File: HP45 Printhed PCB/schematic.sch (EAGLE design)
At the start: 38 parts, among them J1 87224-1, J10 640454-5, J2 87224-1, J3 87224-1, J4 87224-1, J5 87224-1, J6 87224-1, J7 87224-1, J8 87224-1, J9 87224-1, P1 282837-2, Q1 L78M05CDT, U11 DMG1013UWQ-7, U12 DMG1013UWQ-7, U13 DMG1013UWQ-7, U14 DMG1013UWQ-7, U15 DMG1013UWQ-7, U16 DMG1013UWQ-7, U17 DMG1013UWQ-7, U18 DMG1013UWQ-7, U2 CD4504BPWE4, U3 CD4504BPWE4

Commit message: PCB
Completed board 1.0
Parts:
- added R11, R12: 1000Ω, resistor:R-US_R0603
- C1, C2, C3, C4, C5: device capacitor-wima:C2,5-3 -> rcl:C-USC0603
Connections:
- net PIC_MCLR renamed PICKIT_MCLR
- removed net PIC_VDD: C5.1, J10.2, PIC.VDD
- removed net VO: C2.1, Q1.OUT, R2.2
- new net N$12: PIC.RB5, PIC.RC2, PIC.RC4/D-, PIC.RC5/D+, PIC.RC6, PIC.RC7, R12.1
- new net N$3: PIC.RA4, PIC.RA5, PIC.RA6, PIC.RA7, PIC.RB0, R11.2
- new net PICKIT_VDD: C2.1, C5.1, J10.2, PIC.VDD, Q1.OUT, R2.2
- net GND: now also R11.1, R12.2, U2.EIN, U2.FIN, U3.EIN, U3.FIN

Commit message: GRB File
GRB File made and some changes to PCB (Spring loaded pins, names)
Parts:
- C1, C2, C4, C5: MPN (none) -> B32529C0104J000; OC_NEWARK (none) -> 26M8219
- C3, L78M05CDT, MOSFET1, MOSFET3, MOSFET4, MOSFET5, MOSFET6, MOSFET7, MOSFET8, P1, PIC18F, PROGRAMMER, R1, R10, R11, R12, R2, R3, R4, R5, R6, R7, R8, R9, U11, VSHIFTER1, VSHIFTER2: OC_NEWARK (none) -> unknown
- J1, J2, J3, J4, J5, J6, J7, J8, J9: value 87224-1 -> 0926-1-15-20-75-14-11-0; device 87224-1:87224-1 -> 0926-1-15-20-75-14-11-0:0926-1-15-20-75-14-11-0; OC_NEWARK (none) -> unknown
- renumbered J10 to PROGRAMMER, PIC to PIC18F, Q1 to L78M05CDT, U12 to MOSFET4, U13 to MOSFET6, U14 to MOSFET8, U15 to MOSFET1, U16 to MOSFET3, U17 to MOSFET5, U18 to MOSFET7, U2 to VSHIFTER1, U3 to VSHIFTER2

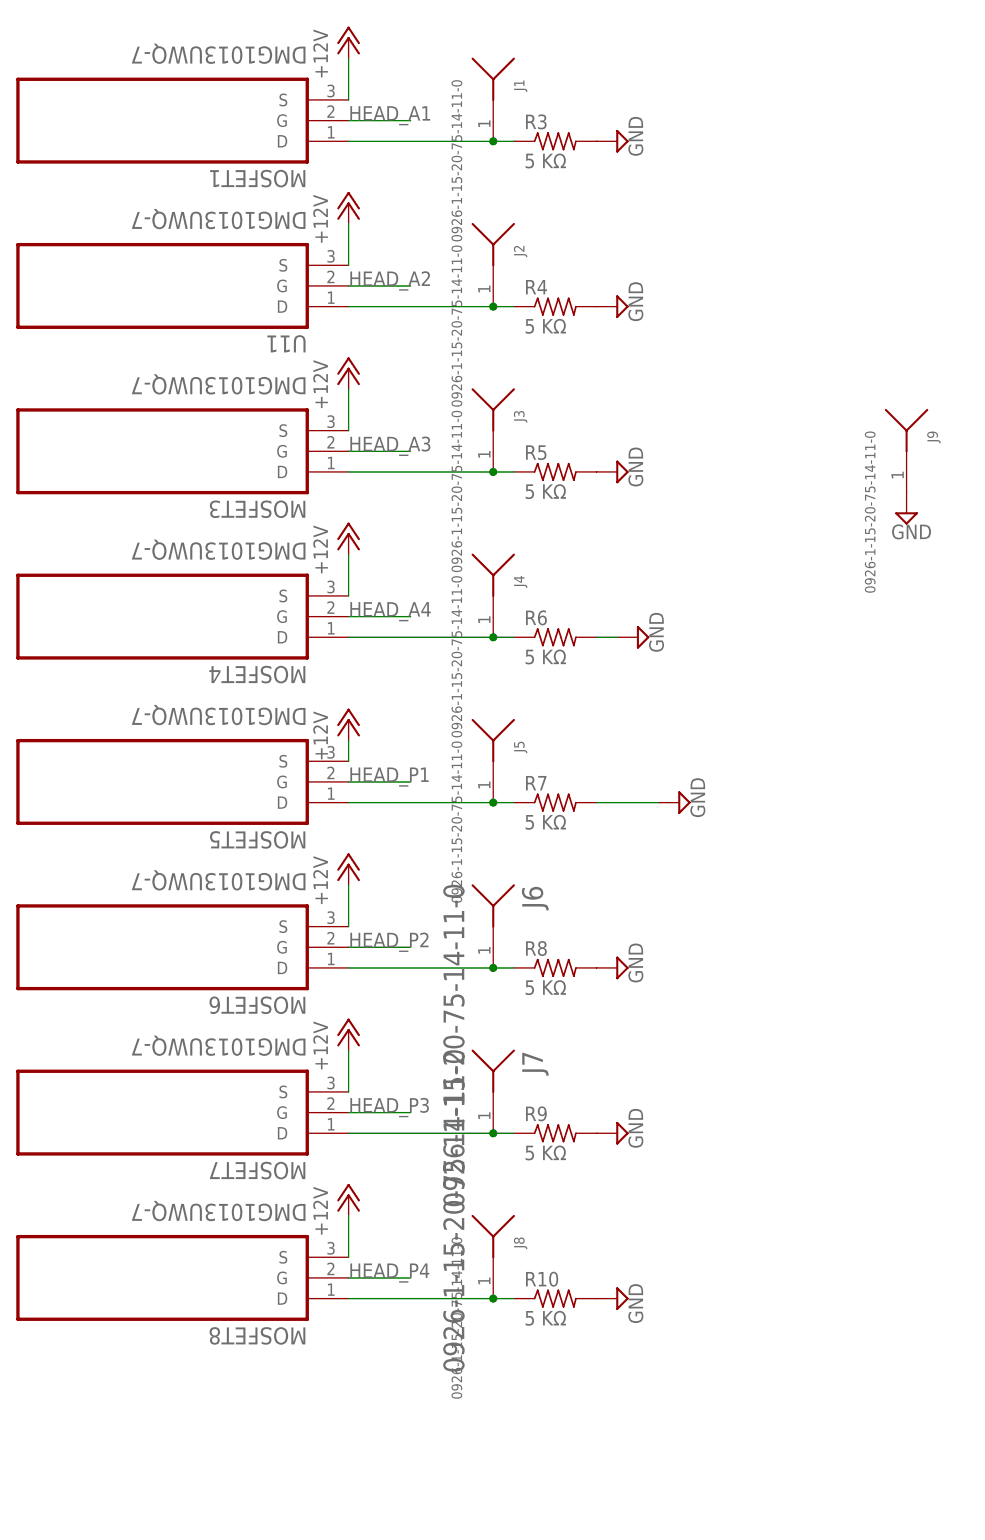
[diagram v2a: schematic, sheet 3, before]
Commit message: PCB Changes
Revised pinheads, modified libraries
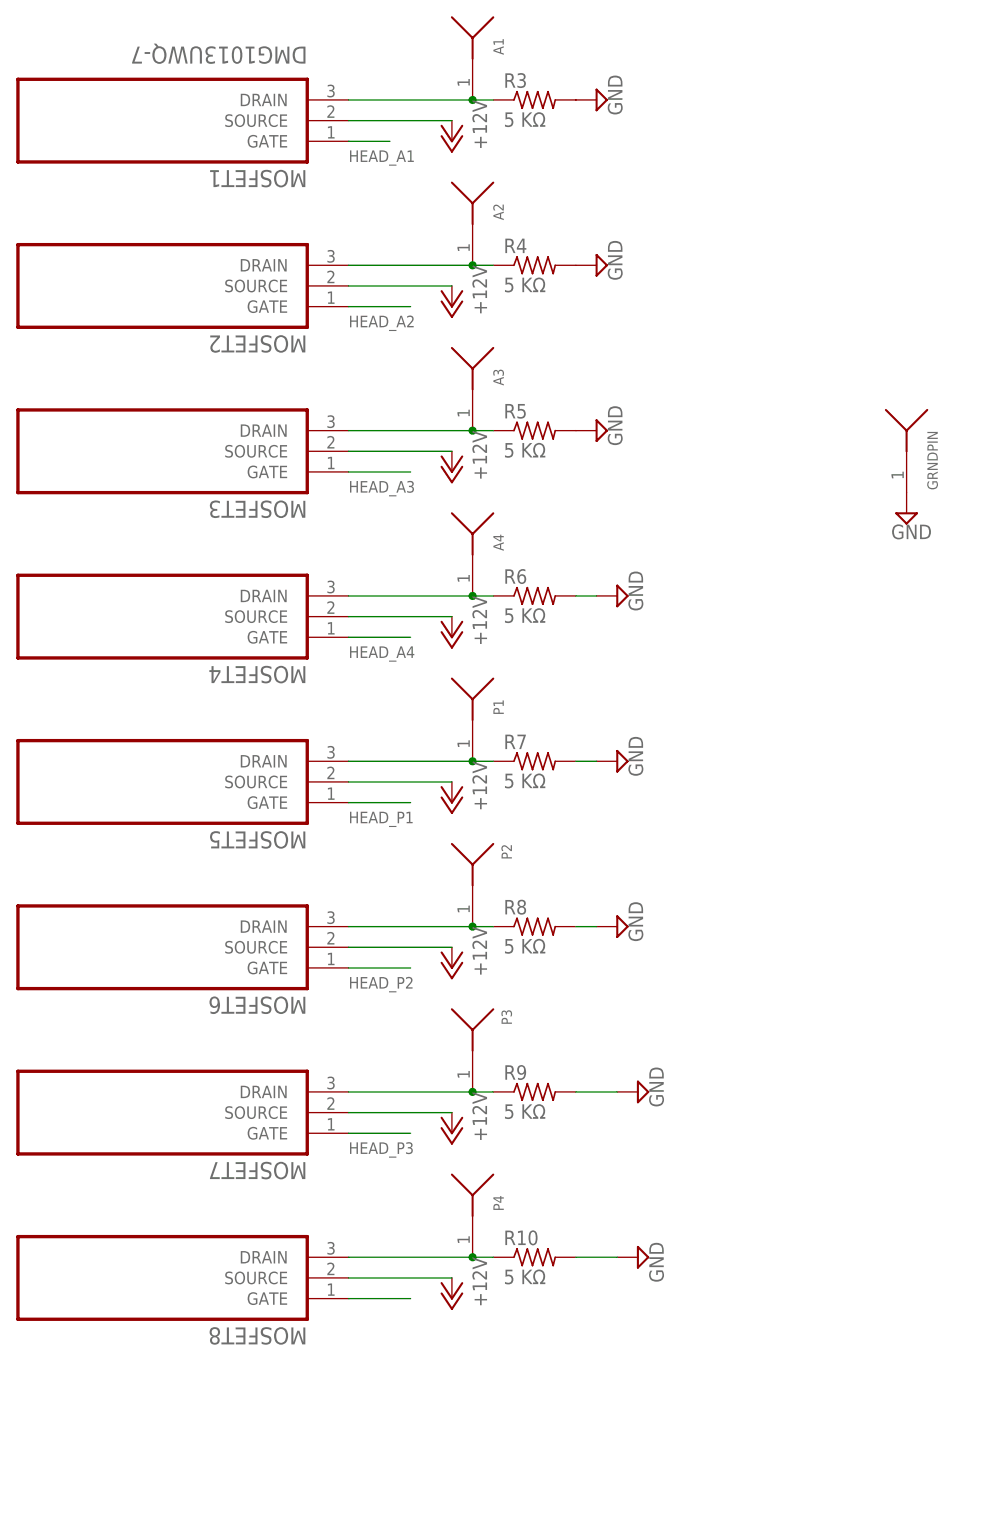
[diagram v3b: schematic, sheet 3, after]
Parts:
- removed J1, J2, J3, J4, J5, J6, J7, J8, J9: 0926-1-15-20-75-14-11-0, 0926-1-15-20-75-14-11-0:0926-1-15-20-75-14-11-0
- added A1, A2, A3, A4, GRNDPIN, P2, P3, P4: 0930, 0930:0930
- added POWER: 282837-2, 282837-2:282837-2
- L78M05CDT: OC_NEWARK unknown -> (none)
- P1: value 282837-2 -> 0930; device 282837-2:282837-2 -> 0930:0930
- renumbered U11 to MOSFET2
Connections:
- net +12V: now also MOSFET1.SOURCE, MOSFET2.SOURCE, MOSFET3.SOURCE, MOSFET4.SOURCE, MOSFET5.SOURCE, MOSFET6.SOURCE, MOSFET7.SOURCE, MOSFET8.SOURCE, POWER.1, VSHIFTER1.VDD, VSHIFTER2.VDD; no longer MOSFET1.S, MOSFET2.S, MOSFET3.S, MOSFET4.S, MOSFET5.S, MOSFET6.S, MOSFET7.S, MOSFET8.S, P1.1, VSHIFTER1.SELECT, VSHIFTER2.SELECT
- net GND: now also GRNDPIN.1, POWER.2; no longer J9.1, P1.2
- net HEAD_A1: now also MOSFET1.GATE; no longer MOSFET1.G
- net HEAD_A2: now also MOSFET2.GATE; no longer MOSFET2.G
- net HEAD_A3: now also MOSFET3.GATE; no longer MOSFET3.G
- net HEAD_A4: now also MOSFET4.GATE; no longer MOSFET4.G
- net HEAD_P1: now also MOSFET5.GATE; no longer MOSFET5.G
- net HEAD_P2: now also MOSFET6.GATE; no longer MOSFET6.G
- net HEAD_P3: now also MOSFET7.GATE; no longer MOSFET7.G
- net HEAD_P4: now also MOSFET8.GATE; no longer MOSFET8.G
- net N$10: now also MOSFET7.DRAIN, P3.1; no longer J7.1, MOSFET7.D
- net N$11: now also MOSFET8.DRAIN, P4.1; no longer J8.1, MOSFET8.D
- net N$2: now also A1.1, MOSFET1.DRAIN; no longer J1.1, MOSFET1.D
- net N$4: now also A2.1, MOSFET2.DRAIN; no longer J2.1, MOSFET2.D
- net N$5: now also A3.1, MOSFET3.DRAIN; no longer J3.1, MOSFET3.D
- net N$7: now also A4.1, MOSFET4.DRAIN; no longer J4.1, MOSFET4.D
- net N$8: now also MOSFET5.DRAIN, P1.1; no longer J5.1, MOSFET5.D
- net N$9: now also MOSFET6.DRAIN, P2.1; no longer J6.1, MOSFET6.D
- net PICKIT_VDD: no longer L78M05CDT.OUT
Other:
- moved on the sheet: C2, C3, C4, C5, R10, R3, R4, R5, R6, R7, R8, R9

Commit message: PCB
Done
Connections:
- net PICKIT_VDD: now also L78M05CDT.OUT
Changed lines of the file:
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@@
 <net name="+12V" class="0">
 <segment>
-<wire x1="-17.78" y1="55.88" x2="7.62" y2="55.88" width="0.1524" layer="91"/>
+<wire x1="-17.78" y1="55.88" x2="10.16" y2="55.88" width="0.1524" layer="91"/>
+<pinref part="P+2" gate="1" pin="+12V"/>
+<pinref part="L78M05CDT" gate="A" pin="IN"/>
 <pinref part="C3" gate="G$1" pin="2"/>
-<wire x1="7.62" y1="55.88" x2="7.62" y2="53.34" width="0.1524" layer="91"/>
-<pinref part="P+2" gate="1" pin="+12V"/>
-<wire x1="7.62" y1="55.88" x2="10.16" y2="55.88" width="0.1524" layer="91"/>
-<junction x="7.62" y="55.88"/>
-<pinref part="L78M05CDT" gate="A" pin="IN"/>
+<wire x1="7.62" y1="53.34" x2="7.62" y2="55.88" width="0.1524" layer="91"/>
+<wire x1="7.62" y1="55.88" x2="-17.78" y2="55.88" width="0.1524" layer="91"/>
+<junction x="-17.78" y="55.88"/>
 </segment>
 <segment>
@@
 <segment>
 <pinref part="C2" gate="G$1" pin="1"/>
-<wire x1="-12.7" y1="50.8" x2="-17.78" y2="50.8" width="0.1524" layer="91"/>
-<wire x1="-12.7" y1="45.72" x2="-12.7" y2="50.8" width="0.1524" layer="91"/>
 <label x="-17.78" y="50.8" size="1.778" layer="95"/>
+<wire x1="-12.7" y1="50.8" x2="-7.62" y2="50.8" width="0.1524" layer="91"/>
+<wire x1="-12.7" y1="50.8" x2="-12.7" y2="45.72" width="0.1524" layer="91"/>
+<pinref part="L78M05CDT" gate="A" pin="OUT"/>
+<wire x1="-17.78" y1="50.8" x2="-12.7" y2="50.8" width="0.1524" layer="91"/>
+<junction x="-12.7" y="50.8"/>
 </segment>
 </net>
@@
 <pinref part="MOSFET8" gate="G$1" pin="GATE"/>
 <wire x1="-5.08" y1="-76.2" x2="2.54" y2="-76.2" width="0.1524" layer="91"/>
-</segment>
-</net>
+<label x="-5.08" y="-78.74" size="1.4224" layer="95"/>
+</segment>
+</net>

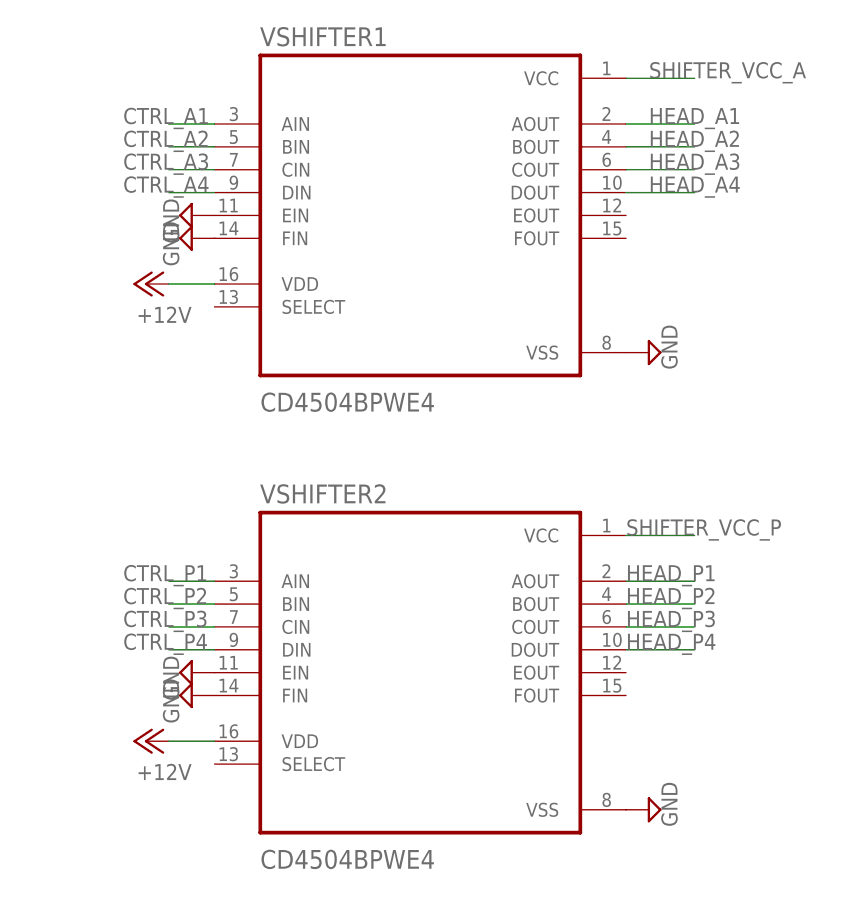
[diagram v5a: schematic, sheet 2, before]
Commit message: Minor FIx
PCB - added Select pin from Shifter to Low Logic with 10Ω Resistor intermeditate
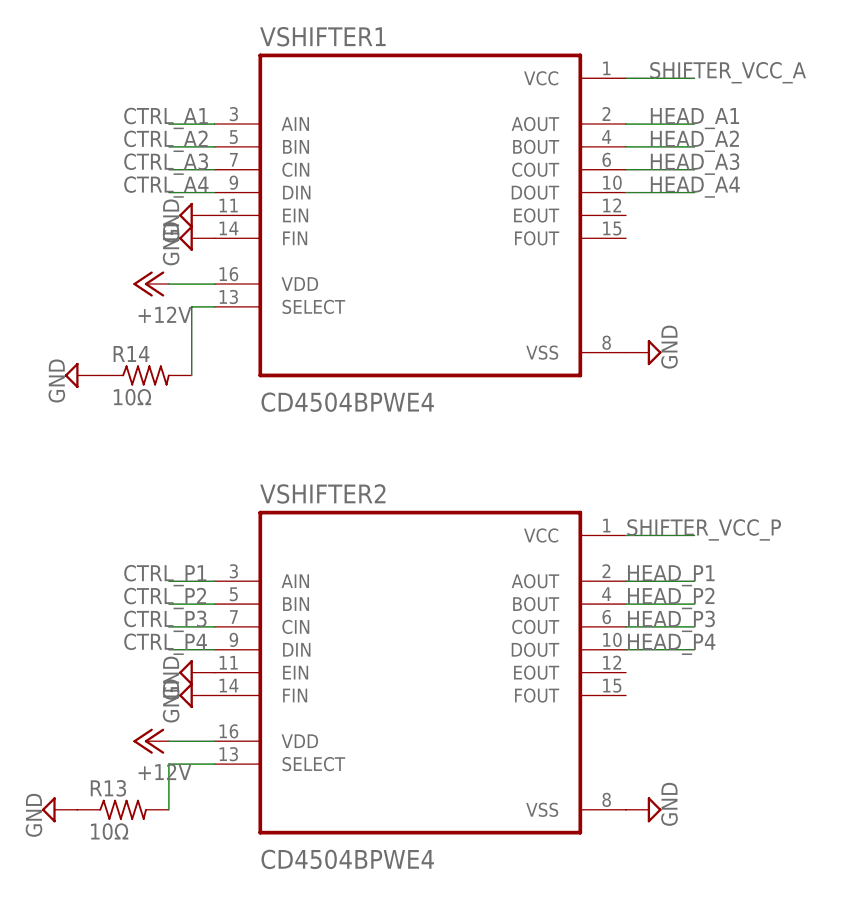
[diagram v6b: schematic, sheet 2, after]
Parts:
- added R13, R14: 10Ω, rcl:R-US_R0603
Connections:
- new net N$13: R14.2, VSHIFTER1.SELECT
- new net N$14: R13.2, VSHIFTER2.SELECT
- net GND: now also R13.1, R14.1
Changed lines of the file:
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@@
 <part name="SUPPLY24" library="supply2" library_urn="urn:adsk.eagle:library:372" deviceset="GND" device=""/>
 <part name="L78M05CDT" library="L78M05CDT" deviceset="L78M05CDT" device=""/>
+<part name="R13" library="rcl" library_urn="urn:adsk.eagle:library:334" deviceset="R-US_" device="R0603" package3d_urn="urn:adsk.eagle:package:23555/2" value="10Ω"/>
+<part name="R14" library="rcl" library_urn="urn:adsk.eagle:library:334" deviceset="R-US_" device="R0603" package3d_urn="urn:adsk.eagle:package:23555/2" value="10Ω"/>
+<part name="SUPPLY25" library="supply2" library_urn="urn:adsk.eagle:library:372" deviceset="GND" device=""/>
+<part name="SUPPLY26" library="supply2" library_urn="urn:adsk.eagle:library:372" deviceset="GND" device=""/>
 </parts>
 <sheets>
@@
 <instance part="SUPPLY23" gate="GND" x="-25.4" y="-53.34" rot="R270"/>
 <instance part="SUPPLY24" gate="GND" x="-25.4" y="-50.8" rot="R270"/>
+<instance part="R13" gate="G$1" x="-33.02" y="-66.04"/>
+<instance part="R14" gate="G$1" x="-30.48" y="-17.78"/>
+<instance part="SUPPLY25" gate="GND" x="-38.1" y="-17.78" rot="R270"/>
+<instance part="SUPPLY26" gate="GND" x="-40.64" y="-66.04" rot="R270"/>
 </instances>
 <busses>
@@
 <pinref part="SUPPLY24" gate="GND" pin="GND"/>
 </segment>
+<segment>
+<pinref part="R14" gate="G$1" pin="1"/>
+<pinref part="SUPPLY25" gate="GND" pin="GND"/>
+</segment>
+<segment>
+<pinref part="R13" gate="G$1" pin="1"/>
+<pinref part="SUPPLY26" gate="GND" pin="GND"/>
+</segment>
 </net>
 <net name="SHIFTER_VCC_A" class="0">
@@
 </segment>
 </net>
+<net name="N$13" class="0">
+<segment>
+<pinref part="R14" gate="G$1" pin="2"/>
+<pinref part="VSHIFTER1" gate="G$1" pin="SELECT"/>
+<wire x1="-25.4" y1="-17.78" x2="-25.4" y2="-10.16" width="0.1524" layer="91"/>
+<wire x1="-25.4" y1="-10.16" x2="-22.86" y2="-10.16" width="0.1524" layer="91"/>
+</segment>
+</net>
+<net name="N$14" class="0">
+<segment>
+<pinref part="R13" gate="G$1" pin="2"/>
+<pinref part="VSHIFTER2" gate="G$1" pin="SELECT"/>
+<wire x1="-27.94" y1="-66.04" x2="-27.94" y2="-60.96" width="0.1524" layer="91"/>
+<wire x1="-27.94" y1="-60.96" x2="-22.86" y2="-60.96" width="0.1524" layer="91"/>
+</segment>
+</net>
